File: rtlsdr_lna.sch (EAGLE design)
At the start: 18 parts, among them U1 MIC5205-3

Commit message: reduced board size, increased clearances, changed voltage regulator footprint, added silkscreen and annotations
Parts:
- U1: device SparkFun-PowerIC:V_REG_LDOSMD2 -> SparkFun-PowerIC:V_REG_LDOSMD
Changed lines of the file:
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@@
 <grid distance="0.1" unitdist="inch" unit="inch" style="lines" multiple="1" display="no" altdistance="0.01" altunitdist="inch" altunit="inch"/>
 <layers>
-<layer number="1" name="Top" color="4" fill="1" visible="no" active="no"/>
-<layer number="16" name="Bottom" color="1" fill="1" visible="no" active="no"/>
-<layer number="17" name="Pads" color="2" fill="1" visible="no" active="no"/>
-<layer number="18" name="Vias" color="2" fill="1" visible="no" active="no"/>
-<layer number="19" name="Unrouted" color="6" fill="1" visible="no" active="no"/>
-<layer number="20" name="Dimension" color="15" fill="1" visible="no" active="no"/>
-<layer number="21" name="tPlace" color="7" fill="1" visible="no" active="no"/>
-<layer number="22" name="bPlace" color="7" fill="1" visible="no" active="no"/>
-<layer number="23" name="tOrigins" color="15" fill="1" visible="no" active="no"/>
-<layer number="24" name="bOrigins" color="15" fill="1" visible="no" active="no"/>
-<layer number="25" name="tNames" color="7" fill="1" visible="no" active="no"/>
-<layer number="26" name="bNames" color="7" fill="1" visible="no" active="no"/>
-<layer number="27" name="tValues" color="7" fill="1" visible="no" active="no"/>
-<layer number="28" name="bValues" color="7" fill="1" visible="no" active="no"/>
+<layer number="1" name="Top" color="4" fill="1" visible="yes" active="no"/>
+<layer number="16" name="Bottom" color="1" fill="1" visible="yes" active="no"/>
+<layer number="17" name="Pads" color="2" fill="1" visible="yes" active="no"/>
+<layer number="18" name="Vias" color="2" fill="1" visible="yes" active="no"/>
+<layer number="19" name="Unrouted" color="6" fill="1" visible="yes" active="no"/>
+<layer number="20" name="Dimension" color="15" fill="1" visible="yes" active="no"/>
+<layer number="21" name="tPlace" color="7" fill="1" visible="yes" active="no"/>
+<layer number="22" name="bPlace" color="7" fill="1" visible="yes" active="no"/>
+<layer number="23" name="tOrigins" color="15" fill="1" visible="yes" active="no"/>
+<layer number="24" name="bOrigins" color="15" fill="1" visible="yes" active="no"/>
+<layer number="25" name="tNames" color="7" fill="1" visible="yes" active="no"/>
+<layer number="26" name="bNames" color="7" fill="1" visible="yes" active="no"/>
+<layer number="27" name="tValues" color="7" fill="1" visible="yes" active="no"/>
+<layer number="28" name="bValues" color="7" fill="1" visible="yes" active="no"/>
 <layer number="29" name="tStop" color="7" fill="3" visible="no" active="no"/>
 <layer number="30" name="bStop" color="7" fill="6" visible="no" active="no"/>
@@
 <layer number="35" name="tGlue" color="7" fill="4" visible="no" active="no"/>
 <layer number="36" name="bGlue" color="7" fill="5" visible="no" active="no"/>
-<layer number="37" name="tTest" color="7" fill="1" visible="no" active="no"/>
-<layer number="38" name="bTest" color="7" fill="1" visible="no" active="no"/>
+<layer number="37" name="tTest" color="7" fill="1" visible="yes" active="no"/>
+<layer number="38" name="bTest" color="7" fill="1" visible="yes" active="no"/>
 <layer number="39" name="tKeepout" color="4" fill="11" visible="no" active="no"/>
 <layer number="40" name="bKeepout" color="1" fill="11" visible="no" active="no"/>
@@
 <layer number="44" name="Drills" color="7" fill="1" visible="no" active="no"/>
 <layer number="45" name="Holes" color="7" fill="1" visible="no" active="no"/>
-<layer number="46" name="Milling" color="3" fill="1" visible="no" active="no"/>
-<layer number="47" name="Measures" color="7" fill="1" visible="no" active="no"/>
-<layer number="48" name="Document" color="7" fill="1" visible="no" active="no"/>
-<layer number="49" name="Reference" color="7" fill="1" visible="no" active="no"/>
-<layer number="50" name="dxf" color="7" fill="1" visible="no" active="no"/>
-<layer number="51" name="tDocu" color="7" fill="1" visible="no" active="no"/>
-<layer number="52" name="bDocu" color="7" fill="1" visible="no" active="no"/>
-<layer number="53" name="tGND_GNDA" color="7" fill="9" visible="no" active="no"/>
-<layer number="54" name="bGND_GNDA" color="1" fill="9" visible="no" active="no"/>
-<layer number="56" name="wert" color="7" fill="1" visible="no" active="no"/>
+<layer number="46" name="Milling" color="3" fill="1" visible="yes" active="no"/>
+<layer number="47" name="Measures" color="7" fill="1" visible="yes" active="no"/>
+<layer number="48" name="Document" color="7" fill="1" visible="yes" active="no"/>
+<layer number="49" name="Reference" color="7" fill="1" visible="yes" active="no"/>
+<layer number="50" name="dxf" color="7" fill="1" visible="yes" active="no"/>
+<layer number="51" name="tDocu" color="7" fill="1" visible="yes" active="no"/>
+<layer number="52" name="bDocu" color="7" fill="1" visible="yes" active="no"/>
+<layer number="53" name="tGND_GNDA" color="7" fill="9" visible="yes" active="no"/>
+<layer number="54" name="bGND_GNDA" color="1" fill="9" visible="yes" active="no"/>
+<layer number="56" name="wert" color="7" fill="1" visible="yes" active="no"/>
 <layer number="91" name="Nets" color="2" fill="1" visible="yes" active="yes"/>
 <layer number="92" name="Busses" color="1" fill="1" visible="yes" active="yes"/>
@@
 <parts>
 <part name="U$1" library="mr_radar" deviceset="MGA-68563" device=""/>
-<part name="U1" library="SparkFun-PowerIC" deviceset="V_REG_LDO" device="SMD2" value="MIC5205-3"/>
+<part name="U1" library="SparkFun-PowerIC" deviceset="V_REG_LDO" device="SMD" value="MIC5205-3"/>
 <part name="GND1" library="supply1" deviceset="GND" device=""/>
 <part name="R1" library="rcl" deviceset="R-EU_" device="R0402" value="4.3k"/>

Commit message: this time with the new layout and schematic..
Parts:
- C1, C4: value 330pF -> 180pF
- R1: value 4.3k -> 1k
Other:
- note added: "MGA-68263"
- note removed: "MGA-68563"
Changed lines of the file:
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@@
 <grid distance="0.1" unitdist="inch" unit="inch" style="lines" multiple="1" display="no" altdistance="0.01" altunitdist="inch" altunit="inch"/>
 <layers>
-<layer number="1" name="Top" color="4" fill="1" visible="yes" active="no"/>
-<layer number="16" name="Bottom" color="1" fill="1" visible="yes" active="no"/>
-<layer number="17" name="Pads" color="2" fill="1" visible="yes" active="no"/>
-<layer number="18" name="Vias" color="2" fill="1" visible="yes" active="no"/>
-<layer number="19" name="Unrouted" color="6" fill="1" visible="yes" active="no"/>
-<layer number="20" name="Dimension" color="15" fill="1" visible="yes" active="no"/>
-<layer number="21" name="tPlace" color="7" fill="1" visible="yes" active="no"/>
-<layer number="22" name="bPlace" color="7" fill="1" visible="yes" active="no"/>
-<layer number="23" name="tOrigins" color="15" fill="1" visible="yes" active="no"/>
-<layer number="24" name="bOrigins" color="15" fill="1" visible="yes" active="no"/>
-<layer number="25" name="tNames" color="7" fill="1" visible="yes" active="no"/>
-<layer number="26" name="bNames" color="7" fill="1" visible="yes" active="no"/>
-<layer number="27" name="tValues" color="7" fill="1" visible="yes" active="no"/>
-<layer number="28" name="bValues" color="7" fill="1" visible="yes" active="no"/>
+<layer number="1" name="Top" color="4" fill="1" visible="no" active="no"/>
+<layer number="16" name="Bottom" color="1" fill="1" visible="no" active="no"/>
+<layer number="17" name="Pads" color="2" fill="1" visible="no" active="no"/>
+<layer number="18" name="Vias" color="2" fill="1" visible="no" active="no"/>
+<layer number="19" name="Unrouted" color="6" fill="1" visible="no" active="no"/>
+<layer number="20" name="Dimension" color="15" fill="1" visible="no" active="no"/>
+<layer number="21" name="tPlace" color="7" fill="1" visible="no" active="no"/>
+<layer number="22" name="bPlace" color="7" fill="1" visible="no" active="no"/>
+<layer number="23" name="tOrigins" color="15" fill="1" visible="no" active="no"/>
+<layer number="24" name="bOrigins" color="15" fill="1" visible="no" active="no"/>
+<layer number="25" name="tNames" color="7" fill="1" visible="no" active="no"/>
+<layer number="26" name="bNames" color="7" fill="1" visible="no" active="no"/>
+<layer number="27" name="tValues" color="7" fill="1" visible="no" active="no"/>
+<layer number="28" name="bValues" color="7" fill="1" visible="no" active="no"/>
 <layer number="29" name="tStop" color="7" fill="3" visible="no" active="no"/>
 <layer number="30" name="bStop" color="7" fill="6" visible="no" active="no"/>
@@
 <layer number="35" name="tGlue" color="7" fill="4" visible="no" active="no"/>
 <layer number="36" name="bGlue" color="7" fill="5" visible="no" active="no"/>
-<layer number="37" name="tTest" color="7" fill="1" visible="yes" active="no"/>
-<layer number="38" name="bTest" color="7" fill="1" visible="yes" active="no"/>
+<layer number="37" name="tTest" color="7" fill="1" visible="no" active="no"/>
+<layer number="38" name="bTest" color="7" fill="1" visible="no" active="no"/>
 <layer number="39" name="tKeepout" color="4" fill="11" visible="no" active="no"/>
 <layer number="40" name="bKeepout" color="1" fill="11" visible="no" active="no"/>
@@
 <layer number="44" name="Drills" color="7" fill="1" visible="no" active="no"/>
 <layer number="45" name="Holes" color="7" fill="1" visible="no" active="no"/>
-<layer number="46" name="Milling" color="3" fill="1" visible="yes" active="no"/>
-<layer number="47" name="Measures" color="7" fill="1" visible="yes" active="no"/>
-<layer number="48" name="Document" color="7" fill="1" visible="yes" active="no"/>
-<layer number="49" name="Reference" color="7" fill="1" visible="yes" active="no"/>
-<layer number="50" name="dxf" color="7" fill="1" visible="yes" active="no"/>
-<layer number="51" name="tDocu" color="7" fill="1" visible="yes" active="no"/>
-<layer number="52" name="bDocu" color="7" fill="1" visible="yes" active="no"/>
-<layer number="53" name="tGND_GNDA" color="7" fill="9" visible="yes" active="no"/>
-<layer number="54" name="bGND_GNDA" color="1" fill="9" visible="yes" active="no"/>
-<layer number="56" name="wert" color="7" fill="1" visible="yes" active="no"/>
+<layer number="46" name="Milling" color="3" fill="1" visible="no" active="no"/>
+<layer number="47" name="Measures" color="7" fill="1" visible="no" active="no"/>
+<layer number="48" name="Document" color="7" fill="1" visible="no" active="no"/>
+<layer number="49" name="Reference" color="7" fill="1" visible="no" active="no"/>
+<layer number="50" name="dxf" color="7" fill="1" visible="no" active="no"/>
+<layer number="51" name="tDocu" color="7" fill="1" visible="no" active="no"/>
+<layer number="52" name="bDocu" color="7" fill="1" visible="no" active="no"/>
+<layer number="53" name="tGND_GNDA" color="7" fill="9" visible="no" active="no"/>
+<layer number="54" name="bGND_GNDA" color="1" fill="9" visible="no" active="no"/>
+<layer number="56" name="wert" color="7" fill="1" visible="no" active="no"/>
 <layer number="91" name="Nets" color="2" fill="1" visible="yes" active="yes"/>
 <layer number="92" name="Busses" color="1" fill="1" visible="yes" active="yes"/>
@@
 <part name="U1" library="SparkFun-PowerIC" deviceset="V_REG_LDO" device="SMD" value="MIC5205-3"/>
 <part name="GND1" library="supply1" deviceset="GND" device=""/>
-<part name="R1" library="rcl" deviceset="R-EU_" device="R0402" value="4.3k"/>
-<part name="C1" library="rcl" deviceset="C-EU" device="C0402" value="330pF"/>
+<part name="R1" library="rcl" deviceset="R-EU_" device="R0402" value="1k"/>
+<part name="C1" library="rcl" deviceset="C-EU" device="C0402" value="180pF"/>
 <part name="C2" library="rcl" deviceset="C-EU" device="C0402" value="68pF"/>
 <part name="C3" library="rcl" deviceset="C-EU" device="C0402" value="10nF"/>
-<part name="C4" library="rcl" deviceset="C-EU" device="C0402" value="330pF"/>
+<part name="C4" library="rcl" deviceset="C-EU" device="C0402" value="180pF"/>
 <part name="FRAME1" library="frames" deviceset="LETTER_L" device=""/>
 <part name="L1" library="SparkFun-Passives" deviceset="INDUCTOR" device="0603" value="100nH"/>
@@
 <text x="193.04" y="63.5" size="1.778" layer="97" font="vector">(U.fl connector for testing)</text>
 <text x="78.74" y="96.52" size="1.778" layer="97" font="vector">airwire to USB 5V</text>
-<text x="106.68" y="38.1" size="1.778" layer="97">MGA-68563</text>
+<text x="106.68" y="38.1" size="1.778" layer="97">MGA-68263</text>
 <text x="236.22" y="-33.02" size="2.54" layer="94">0</text>
 <text x="147.32" y="-12.7" size="2.54" layer="94" font="vector">LNA for rtl-sdr, 100 MHz to 1.5 GHz</text>

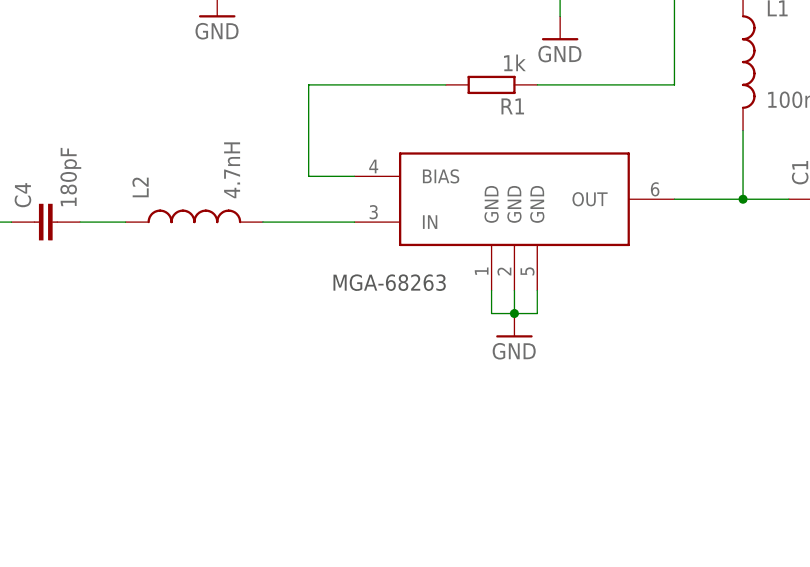
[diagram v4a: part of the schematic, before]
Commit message: cleaned up layout to pass DRC, rtl-sdr-lna ready for manufacturing
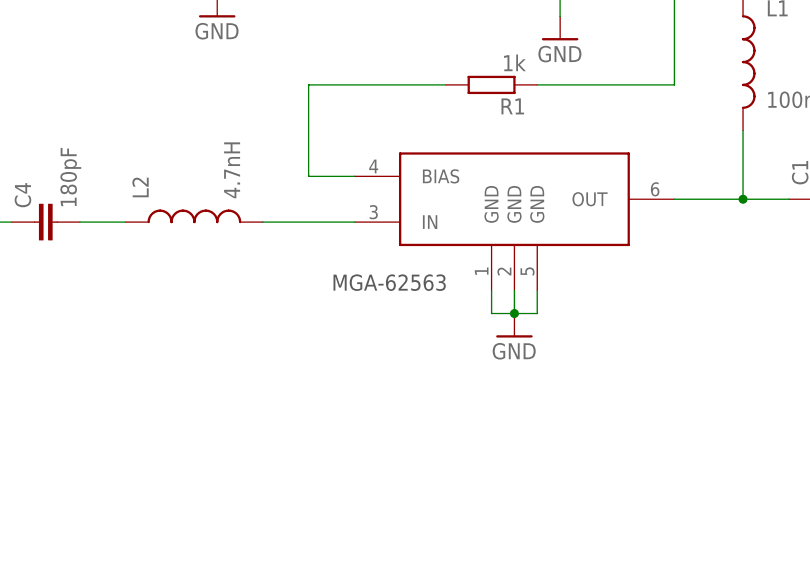
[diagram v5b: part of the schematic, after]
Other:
- note added: "MGA-62563"
- note removed: "MGA-68263"
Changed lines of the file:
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@@
 <text x="193.04" y="63.5" size="1.778" layer="97" font="vector">(U.fl connector for testing)</text>
 <text x="78.74" y="96.52" size="1.778" layer="97" font="vector">airwire to USB 5V</text>
-<text x="106.68" y="38.1" size="1.778" layer="97">MGA-68263</text>
+<text x="106.68" y="38.1" size="1.778" layer="97">MGA-62563</text>
 <text x="236.22" y="-33.02" size="2.54" layer="94">0</text>
 <text x="147.32" y="-12.7" size="2.54" layer="94" font="vector">LNA for rtl-sdr, 100 MHz to 1.5 GHz</text>
